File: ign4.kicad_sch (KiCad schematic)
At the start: 13 parts, among them U1801 MIC4427, U1802 MIC4427

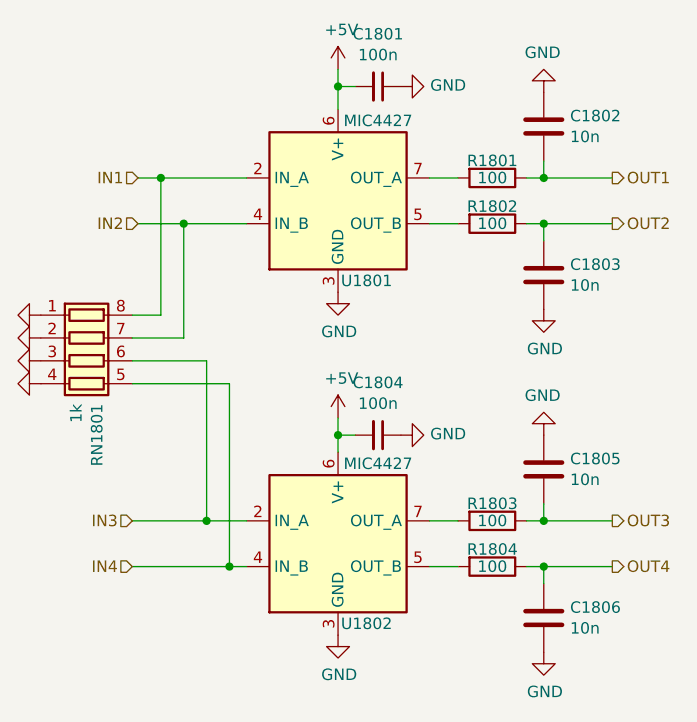
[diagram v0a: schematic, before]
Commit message: Started moving to pin headers
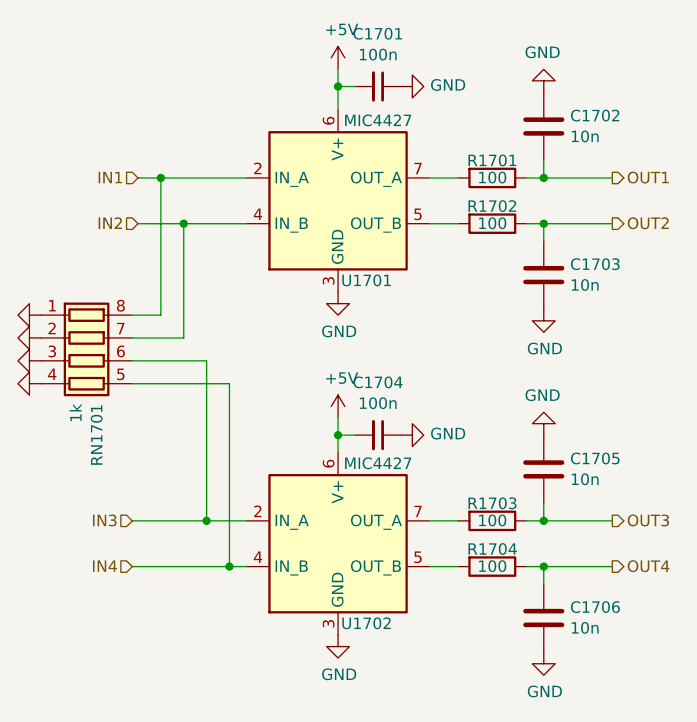
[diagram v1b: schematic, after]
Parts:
- renumbered C1801 to C1701, C1802 to C1702, C1803 to C1703, C1804 to C1704, C1805 to C1705, C1806 to C1706, R1801 to R1701, R1802 to R1702, R1803 to R1703, R1804 to R1704, RN1801 to RN1701, U1801 to U1701, U1802 to U1702
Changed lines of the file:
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@@
   (symbol (lib_id "Driver_FET:MIC4427") (at 76.835 46.99 0)
     (in_bom yes) (on_board yes)
-    (property "Reference" "U1801" (id 0) (at 80.01 55.88 0))
+    (property "Reference" "U1701" (id 0) (at 80.01 55.88 0))
     (property "Value" "MIC4427" (id 1) (at 81.28 38.1 0))
     (property "Footprint" "Package_SO:SOIC-8_3.9x4.9mm_P1.27mm" (id 2) (at 76.835 54.61 0)
@@
   (symbol (lib_id "Driver_FET:MIC4427") (at 76.835 85.09 0)
     (in_bom yes) (on_board yes)
-    (property "Reference" "U1802" (id 0) (at 80.01 93.98 0))
+    (property "Reference" "U1702" (id 0) (at 80.01 93.98 0))
     (property "Value" "MIC4427" (id 1) (at 81.28 76.2 0))
     (property "Footprint" "Package_SO:SOIC-8_3.9x4.9mm_P1.27mm" (id 2) (at 76.835 92.71 0)
@@
   (symbol (lib_id "Device:C_Small") (at 81.28 73.025 270)
     (in_bom yes) (on_board yes)
-    (property "Reference" "C1804" (id 0) (at 81.28 67.2084 90))
+    (property "Reference" "C1704" (id 0) (at 81.28 67.2084 90))
     (property "Value" "100n" (id 1) (at 81.28 69.5198 90))
     (property "Footprint" "Capacitor_SMD:C_0603_1608Metric" (id 2) (at 81.28 73.025 0)
@@
   (symbol (lib_id "Device:C_Small") (at 81.28 34.29 270)
     (in_bom yes) (on_board yes)
-    (property "Reference" "C1801" (id 0) (at 81.28 28.4734 90))
+    (property "Reference" "C1701" (id 0) (at 81.28 28.4734 90))
     (property "Value" "100n" (id 1) (at 81.28 30.7848 90))
     (property "Footprint" "Capacitor_SMD:C_0603_1608Metric" (id 2) (at 81.28 34.29 0)
@@
   (symbol (lib_id "Device:R") (at 93.98 44.45 270)
     (in_bom yes) (on_board yes)
-    (property "Reference" "R1801" (id 0) (at 93.98 42.545 90))
+    (property "Reference" "R1701" (id 0) (at 93.98 42.545 90))
     (property "Value" "100" (id 1) (at 93.98 44.45 90))
     (property "Footprint" "Resistor_SMD:R_0805_2012Metric" (id 2) (at 93.98 42.672 90)
@@
   (symbol (lib_id "Device:R") (at 93.98 49.53 270)
     (in_bom yes) (on_board yes)
-    (property "Reference" "R1802" (id 0) (at 93.98 47.625 90))
+    (property "Reference" "R1702" (id 0) (at 93.98 47.625 90))
     (property "Value" "100" (id 1) (at 93.98 49.53 90))
     (property "Footprint" "Resistor_SMD:R_0805_2012Metric" (id 2) (at 93.98 47.752 90)
@@
   (symbol (lib_id "Device:R") (at 93.98 82.55 270)
     (in_bom yes) (on_board yes)
-    (property "Reference" "R1803" (id 0) (at 93.98 80.645 90))
+    (property "Reference" "R1703" (id 0) (at 93.98 80.645 90))
     (property "Value" "100" (id 1) (at 93.98 82.55 90))
     (property "Footprint" "Resistor_SMD:R_0805_2012Metric" (id 2) (at 93.98 80.772 90)
@@
   (symbol (lib_id "Device:R") (at 93.98 87.63 270)
     (in_bom yes) (on_board yes)
-    (property "Reference" "R1804" (id 0) (at 93.98 85.725 90))
+    (property "Reference" "R1704" (id 0) (at 93.98 85.725 90))
     (property "Value" "100" (id 1) (at 93.98 87.63 90))
     (property "Footprint" "Resistor_SMD:R_0805_2012Metric" (id 2) (at 93.98 85.852 90)
@@
   (symbol (lib_id "Device:C") (at 99.695 55.245 0)
     (in_bom yes) (on_board yes)
-    (property "Reference" "C1803" (id 0) (at 102.616 54.0766 0)
+    (property "Reference" "C1703" (id 0) (at 102.616 54.0766 0)
       (effects (font (size 1.27 1.27)) (justify left))
     )
@@
   (symbol (lib_id "Device:C") (at 99.695 38.735 180)
     (in_bom yes) (on_board yes)
-    (property "Reference" "C1802" (id 0) (at 102.616 37.5666 0)
+    (property "Reference" "C1702" (id 0) (at 102.616 37.5666 0)
       (effects (font (size 1.27 1.27)) (justify right))
     )
@@
   (symbol (lib_id "Device:C") (at 99.695 76.835 180)
     (in_bom yes) (on_board yes)
-    (property "Reference" "C1805" (id 0) (at 102.616 75.6666 0)
+    (property "Reference" "C1705" (id 0) (at 102.616 75.6666 0)
       (effects (font (size 1.27 1.27)) (justify right))
     )
@@
   (symbol (lib_id "Device:C") (at 99.695 93.345 0)
     (in_bom yes) (on_board yes)
-    (property "Reference" "C1806" (id 0) (at 102.616 92.1766 0)
+    (property "Reference" "C1706" (id 0) (at 102.616 92.1766 0)
       (effects (font (size 1.27 1.27)) (justify left))
     )
@@
   (symbol (lib_id "Device:R_Pack04") (at 48.895 64.77 270)
     (in_bom yes) (on_board yes)
-    (property "Reference" "RN1801" (id 0) (at 50.0634 69.5452 0)
+    (property "Reference" "RN1701" (id 0) (at 50.0634 69.5452 0)
       (effects (font (size 1.27 1.27)) (justify left))
     )

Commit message: Stuff
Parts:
- renumbered C1701 to C1604, C1702 to C1605, C1703 to C1606, C1704 to C1607, C1705 to C1608, C1706 to C1609, R1701 to R1601, R1702 to R1602, R1703 to R1603, R1704 to R1604, RN1701 to RN1601, U1701 to U1602, U1702 to U1603
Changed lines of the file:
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@@
   (symbol (lib_id "Driver_FET:MIC4427") (at 76.835 46.99 0)
     (in_bom yes) (on_board yes)
-    (property "Reference" "U1701" (id 0) (at 80.01 55.88 0))
+    (property "Reference" "U1602" (id 0) (at 80.01 55.88 0))
     (property "Value" "MIC4427" (id 1) (at 81.28 38.1 0))
     (property "Footprint" "Package_SO:SOIC-8_3.9x4.9mm_P1.27mm" (id 2) (at 76.835 54.61 0)
@@
   (symbol (lib_id "Driver_FET:MIC4427") (at 76.835 85.09 0)
     (in_bom yes) (on_board yes)
-    (property "Reference" "U1702" (id 0) (at 80.01 93.98 0))
+    (property "Reference" "U1603" (id 0) (at 80.01 93.98 0))
     (property "Value" "MIC4427" (id 1) (at 81.28 76.2 0))
     (property "Footprint" "Package_SO:SOIC-8_3.9x4.9mm_P1.27mm" (id 2) (at 76.835 92.71 0)
@@
   (symbol (lib_id "Device:C_Small") (at 81.28 73.025 270)
     (in_bom yes) (on_board yes)
-    (property "Reference" "C1704" (id 0) (at 81.28 67.2084 90))
+    (property "Reference" "C1607" (id 0) (at 81.28 67.2084 90))
     (property "Value" "100n" (id 1) (at 81.28 69.5198 90))
     (property "Footprint" "Capacitor_SMD:C_0603_1608Metric" (id 2) (at 81.28 73.025 0)
@@
   (symbol (lib_id "Device:C_Small") (at 81.28 34.29 270)
     (in_bom yes) (on_board yes)
-    (property "Reference" "C1701" (id 0) (at 81.28 28.4734 90))
+    (property "Reference" "C1604" (id 0) (at 81.28 28.4734 90))
     (property "Value" "100n" (id 1) (at 81.28 30.7848 90))
     (property "Footprint" "Capacitor_SMD:C_0603_1608Metric" (id 2) (at 81.28 34.29 0)
@@
   (symbol (lib_id "Device:R") (at 93.98 44.45 270)
     (in_bom yes) (on_board yes)
-    (property "Reference" "R1701" (id 0) (at 93.98 42.545 90))
+    (property "Reference" "R1601" (id 0) (at 93.98 42.545 90))
     (property "Value" "100" (id 1) (at 93.98 44.45 90))
     (property "Footprint" "Resistor_SMD:R_0805_2012Metric" (id 2) (at 93.98 42.672 90)
@@
   (symbol (lib_id "Device:R") (at 93.98 49.53 270)
     (in_bom yes) (on_board yes)
-    (property "Reference" "R1702" (id 0) (at 93.98 47.625 90))
+    (property "Reference" "R1602" (id 0) (at 93.98 47.625 90))
     (property "Value" "100" (id 1) (at 93.98 49.53 90))
     (property "Footprint" "Resistor_SMD:R_0805_2012Metric" (id 2) (at 93.98 47.752 90)
@@
   (symbol (lib_id "Device:R") (at 93.98 82.55 270)
     (in_bom yes) (on_board yes)
-    (property "Reference" "R1703" (id 0) (at 93.98 80.645 90))
+    (property "Reference" "R1603" (id 0) (at 93.98 80.645 90))
     (property "Value" "100" (id 1) (at 93.98 82.55 90))
     (property "Footprint" "Resistor_SMD:R_0805_2012Metric" (id 2) (at 93.98 80.772 90)
@@
   (symbol (lib_id "Device:R") (at 93.98 87.63 270)
     (in_bom yes) (on_board yes)
-    (property "Reference" "R1704" (id 0) (at 93.98 85.725 90))
+    (property "Reference" "R1604" (id 0) (at 93.98 85.725 90))
     (property "Value" "100" (id 1) (at 93.98 87.63 90))
     (property "Footprint" "Resistor_SMD:R_0805_2012Metric" (id 2) (at 93.98 85.852 90)
@@
   (symbol (lib_id "Device:C") (at 99.695 55.245 0)
     (in_bom yes) (on_board yes)
-    (property "Reference" "C1703" (id 0) (at 102.616 54.0766 0)
+    (property "Reference" "C1606" (id 0) (at 102.616 54.0766 0)
       (effects (font (size 1.27 1.27)) (justify left))
     )
@@
   (symbol (lib_id "Device:C") (at 99.695 38.735 180)
     (in_bom yes) (on_board yes)
-    (property "Reference" "C1702" (id 0) (at 102.616 37.5666 0)
+    (property "Reference" "C1605" (id 0) (at 102.616 37.5666 0)
       (effects (font (size 1.27 1.27)) (justify right))
     )
@@
   (symbol (lib_id "Device:C") (at 99.695 76.835 180)
     (in_bom yes) (on_board yes)
-    (property "Reference" "C1705" (id 0) (at 102.616 75.6666 0)
+    (property "Reference" "C1608" (id 0) (at 102.616 75.6666 0)
       (effects (font (size 1.27 1.27)) (justify right))
     )
@@
   (symbol (lib_id "Device:C") (at 99.695 93.345 0)
     (in_bom yes) (on_board yes)
-    (property "Reference" "C1706" (id 0) (at 102.616 92.1766 0)
+    (property "Reference" "C1609" (id 0) (at 102.616 92.1766 0)
       (effects (font (size 1.27 1.27)) (justify left))
     )
@@
   (symbol (lib_id "Device:R_Pack04") (at 48.895 64.77 270)
     (in_bom yes) (on_board yes)
-    (property "Reference" "RN1701" (id 0) (at 50.0634 69.5452 0)
+    (property "Reference" "RN1601" (id 0) (at 50.0634 69.5452 0)
       (effects (font (size 1.27 1.27)) (justify left))
     )
